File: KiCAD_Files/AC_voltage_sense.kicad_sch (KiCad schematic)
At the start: 18 parts, among them U501 AMC1301DWR, U502 MCP6486UT-E/LT

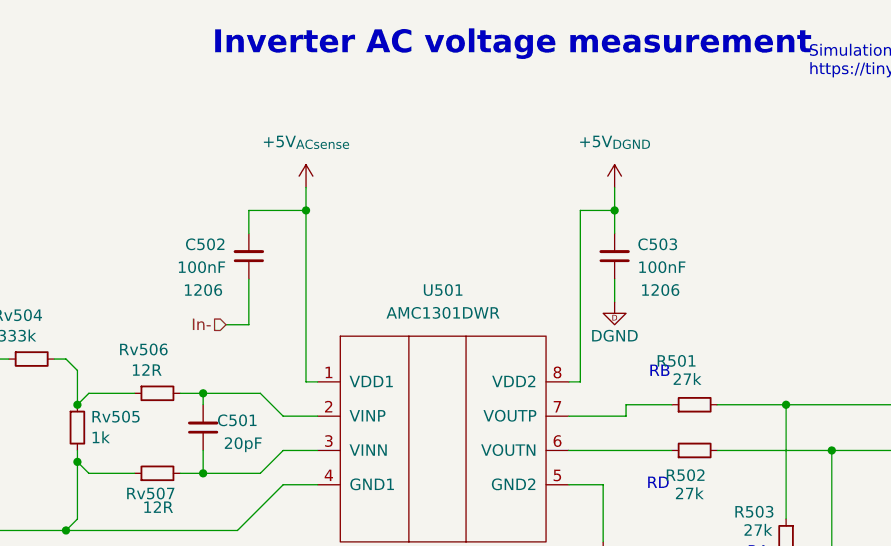
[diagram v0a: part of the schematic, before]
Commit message: First routing pass complete.
Signed-off-by: Jean Alinei <jean.alinei@owntech.org>
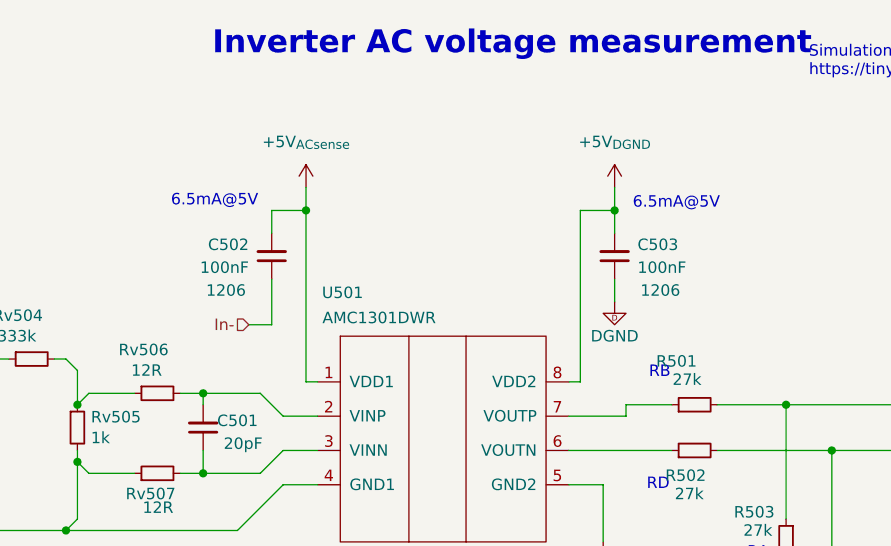
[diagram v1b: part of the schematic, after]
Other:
- note added: "6.5mA@5V"
- moved on the sheet: C502
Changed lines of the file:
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@@
+		)
+	)
+	(text "6.5mA@5V"
+		(exclude_from_sim no)
+		(at 74.93 47.244 0)
+		(effects
+			(font
+				(size 1.27 1.27)
+				(color 194 0 0 1)
+			)
+		)
+	)
+	(text "6.5mA@5V"
+		(exclude_from_sim no)
+		(at 126.238 47.498 0)
+		(effects
+			(font
+				(size 1.27 1.27)
+				(color 194 0 0 1)
+			)
 		)
 	)
@@
 	(wire
 		(pts
-			(xy 78.74 48.26) (xy 78.74 50.8)
+			(xy 81.28 48.26) (xy 81.28 50.8)
 		)
 		(stroke
@@
 	(wire
 		(pts
-			(xy 78.74 60.96) (xy 76.2 60.96)
+			(xy 81.28 60.96) (xy 78.74 60.96)
 		)
 		(stroke
@@
 	(wire
 		(pts
-			(xy 78.74 55.88) (xy 78.74 60.96)
+			(xy 81.28 55.88) (xy 81.28 60.96)
 		)
 		(stroke
@@
 	(wire
 		(pts
-			(xy 78.74 48.26) (xy 85.09 48.26)
+			(xy 81.28 48.26) (xy 85.09 48.26)
 		)
 		(stroke
@@
 	(hierarchical_label "In-"
 		(shape input)
-		(at 76.2 60.96 180)
+		(at 78.74 60.96 180)
 		(effects
 			(font
@@
 			)
 			(justify right)
+		)
+	)
+	(rule_area
+		(polyline
+			(pts
+				(xy 100.33 35.56) (xy 100.33 107.95) (xy 195.58 107.95) (xy 195.58 35.56)
+			)
+			(stroke
+				(width 0)
+				(type dash)
+			)
+			(fill
+				(type none)
+			)
+		)
+	)
+	(netclass_flag ""
+		(length 2.54)
+		(shape round)
+		(at 110.49 107.95 0)
+		(fields_autoplaced yes)
+		(effects
+			(font
+				(size 1.27 1.27)
+			)
+			(justify left bottom)
+		)
+		(property "Netclass" "DGND"
+			(at 111.1885 105.41 0)
+			(effects
+				(font
+					(size 1.27 1.27)
+				)
+				(justify left)
+			)
+		)
+		(property "Component Class" ""
+			(at -148.59 59.69 0)
+			(effects
+				(font
+					(size 1.27 1.27)
+					(italic yes)
+				)
+				(hide yes)
+			)
 		)
 	)
@@
 		(on_board yes)
 		(dnp no)
-		(fields_autoplaced yes)
 		(property "Reference" "U501"
-			(at 100.33 57.15 0)
+			(at 89.154 57.404 0)
 			(effects
 				(font
@@
 		)
 		(property "Value" "AMC1301DWR"
-			(at 100.33 59.69 0)
+			(at 93.218 60.198 0)
 			(effects
 				(font
@@
 			)
 		)
-		(property "Datasheet" "https://www.ti.com/lit/ds/symlink/amc1100.pdf?ts=1597048467257&ref_url=https%253A%252F%252Fwww.google.com%252F"
+		(property "Datasheet" "${KIPRJMOD}\\datasheets\\amc1301.pdf"
 			(at 100.33 81.28 0)
 			(effects
@@
 	(symbol
 		(lib_id "Device:C_Small")
-		(at 78.74 53.34 180)
+		(at 81.28 53.34 180)
 		(unit 1)
 		(exclude_from_sim no)
@@
 		(dnp no)
 		(property "Reference" "C502"
-			(at 76.2 52.07 0)
+			(at 78.74 52.07 0)
 			(effects
 				(font
@@
 		)
 		(property "Value" "100nF"
-			(at 76.2 54.61 0)
+			(at 78.74 54.61 0)
 			(effects
 				(font
@@
 		)
 		(property "Footprint" "Capacitor_SMD:C_1206_3216Metric"
-			(at 78.74 53.34 0)
+			(at 81.28 53.34 0)
 			(effects
 				(font
@@
 		)
 		(property "Datasheet" "${KIPRJMOD}\\datasheet\\KEM_C1002_X7R_SMD-3316098.pdf"
-			(at 78.74 53.34 0)
+			(at 81.28 53.34 0)
 			(effects
 				(font
@@
 		)
 		(property "Description" ""
-			(at 78.74 53.34 0)
+			(at 81.28 53.34 0)
 			(effects
 				(font
@@
 		)
 		(property "manf#" "C1206C104K5RAC7867"
-			(at 78.74 53.34 0)
+			(at 81.28 53.34 0)
 			(effects
 				(font
@@
 		)
 		(property "DNP" ""
-			(at 78.74 53.34 0)
+			(at 81.28 53.34 0)
 			(effects
 				(font
@@
 		)
 		(property "Voltage" "50V"
-			(at 80.01 49.53 90)
+			(at 82.55 49.53 90)
 			(effects
 				(font
@@
 		)
 		(property "Package" "1206"
-			(at 73.66 57.15 0)
+			(at 76.2 57.15 0)
 			(effects
 				(font
@@
 		)
 		(property "Functional Block" "Measurement"
-			(at 78.74 53.34 0)
+			(at 81.28 53.34 0)
 			(effects
 				(font
@@
 		)
 		(property "Metal content" "BaTiO3"
-			(at 78.74 53.34 0)
+			(at 81.28 53.34 0)
 			(effects
 				(font
@@
 		)
 		(property "Subfunction" "VIHigh measure"
-			(at 78.74 53.34 0)
+			(at 81.28 53.34 0)
 			(effects
 				(font
@@
 		)
 		(property "Dielectric" "X7R"
-			(at 78.74 53.34 0)
+			(at 81.28 53.34 0)
 			(effects
 				(font
@@
 		)
 		(property "Technology" ""
-			(at 78.74 53.34 0)
+			(at 81.28 53.34 0)
 			(effects
 				(font
@@
 		)
 		(property "LCSC" "C5449000"
-			(at 78.74 53.34 0)
-			(effects
-				(font
+			(at 81.28 53.34 0)
+			(effects
+				(font

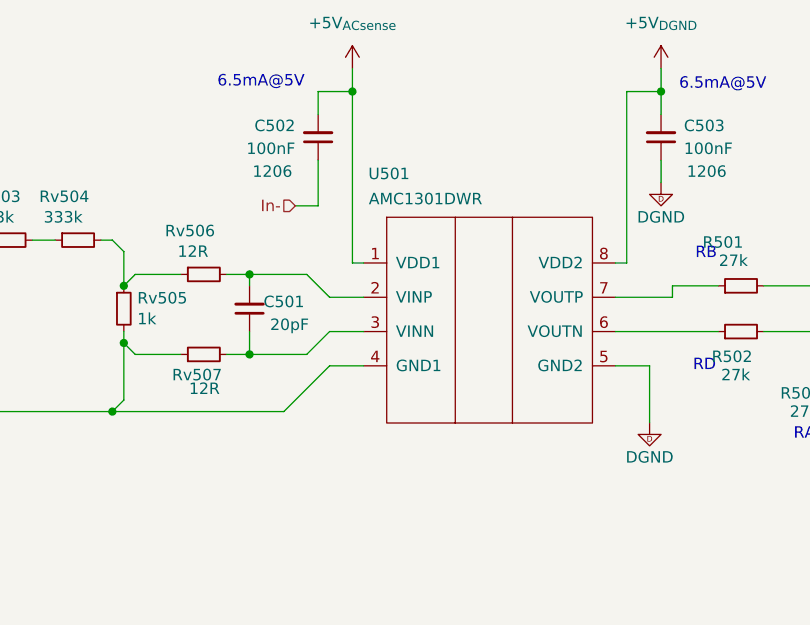
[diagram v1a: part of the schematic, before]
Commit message: Added DRC rules according to IEC60664 and IPC2221.
Signed-off-by: Jean Alinei <jean.alinei@owntech.org>
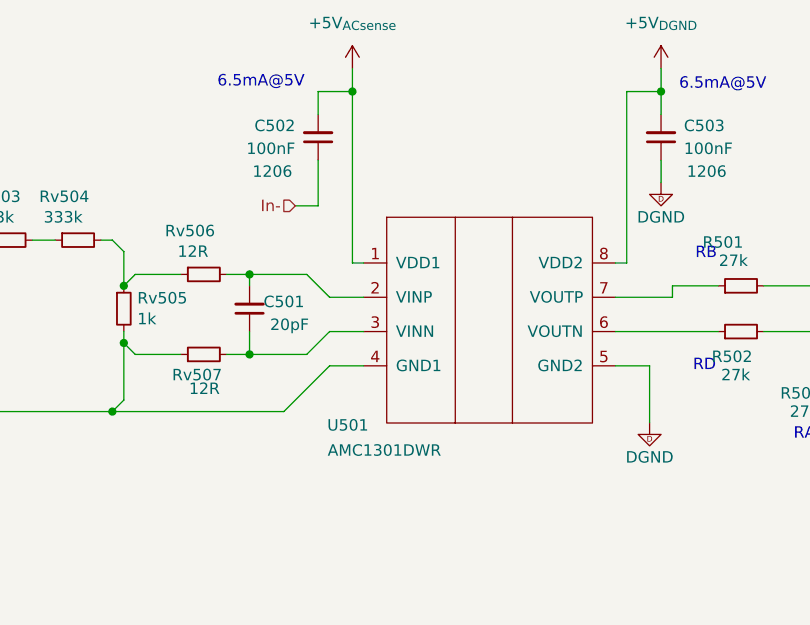
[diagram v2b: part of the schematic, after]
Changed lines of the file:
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@@
 		(polyline
 			(pts
-				(xy 100.33 35.56) (xy 100.33 107.95) (xy 195.58 107.95) (xy 195.58 35.56)
+				(xy 97.79 107.95) (xy 97.79 35.56) (xy 20.32 35.56) (xy 20.32 71.755) (xy 20.32 74.93) (xy 20.32 107.95)
 			)
 			(stroke
@@
 		)
 	)
+	(rule_area
+		(polyline
+			(pts
+				(xy 101.6 35.56) (xy 101.6 107.95) (xy 196.85 107.95) (xy 196.85 35.56)
+			)
+			(stroke
+				(width 0)
+				(type dash)
+			)
+			(fill
+				(type none)
+			)
+		)
+	)
 	(netclass_flag ""
 		(length 2.54)
 		(shape round)
-		(at 110.49 107.95 0)
+		(at 87.63 107.95 0)
 		(fields_autoplaced yes)
 		(effects
@@
 			(justify left bottom)
 		)
+		(property "Netclass" "N"
+			(at 88.3285 105.41 0)
+			(effects
+				(font
+					(size 1.27 1.27)
+				)
+				(justify left)
+			)
+		)
+		(property "Component Class" ""
+			(at -171.45 59.69 0)
+			(effects
+				(font
+					(size 1.27 1.27)
+					(italic yes)
+				)
+				(hide yes)
+			)
+		)
+	)
+	(netclass_flag ""
+		(length 2.54)
+		(shape round)
+		(at 111.76 107.95 0)
+		(fields_autoplaced yes)
+		(effects
+			(font
+				(size 1.27 1.27)
+			)
+			(justify left bottom)
+		)
 		(property "Netclass" "DGND"
-			(at 111.1885 105.41 0)
+			(at 112.4585 105.41 0)
 			(effects
 				(font
@@
 		)
 		(property "Component Class" ""
-			(at -148.59 59.69 0)
+			(at -147.32 59.69 0)
 			(effects
 				(font
@@
 		(dnp no)
 		(property "Reference" "U501"
-			(at 89.154 57.404 0)
+			(at 84.582 85.344 0)
 			(effects
 				(font
@@
 		)
 		(property "Value" "AMC1301DWR"
-			(at 93.218 60.198 0)
-			(effects
-				(font
+			(at 88.646 88.138 0)
+			(effects
+				(font

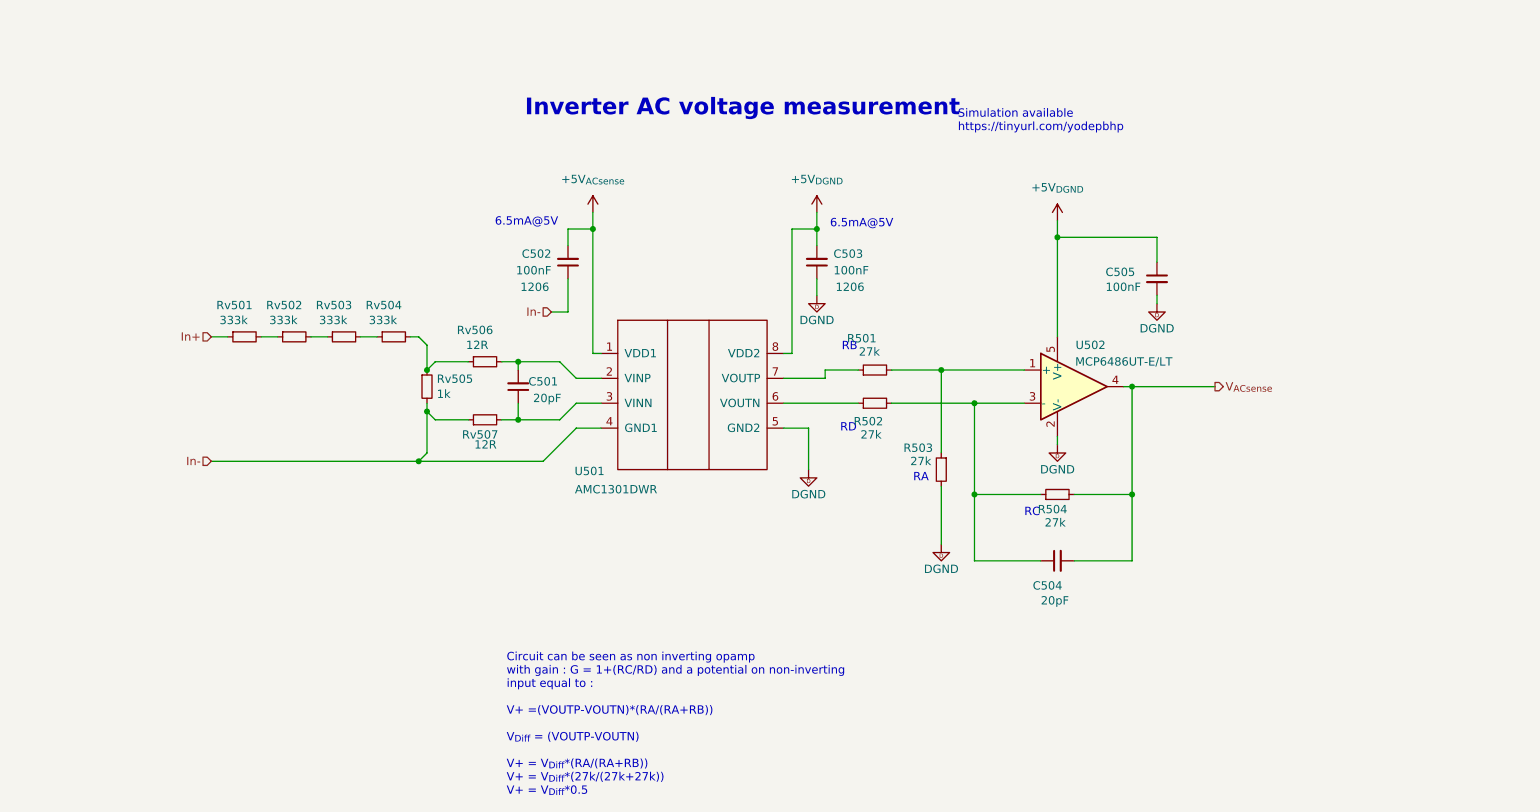
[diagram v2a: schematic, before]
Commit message: Added passive references. Added ESD protection for MCU pins.
Signed-off-by: Jean Alinei <jean.alinei@owntech.org>
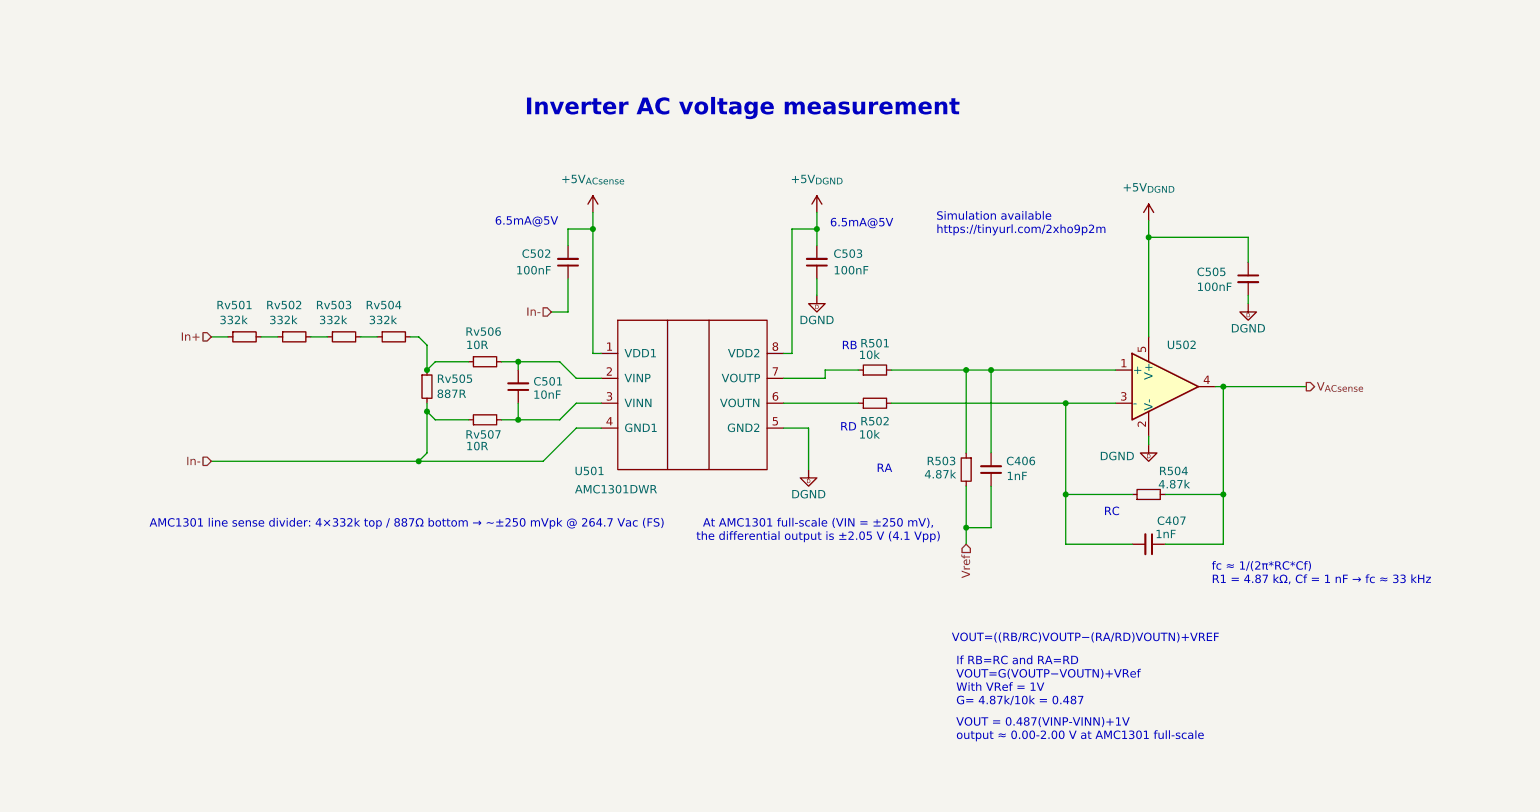
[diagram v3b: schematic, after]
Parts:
- removed C504: 20pF, Footprints:C_0805_2012Metric, symbol Device:C_Small
- added C406, C407: 1nF, Footprints:C_0805_2012Metric, symbol Device:C_Small
- C501: value 20pF -> 10nF; Dielectric NP0 -> (none); LCSC (none) -> C1710; Package 0805 -> (none); Voltage 50V -> (none); manf# CC0805JRNPO9BN200 -> (none)
- C502, C503: Dielectric X7R -> (none); LCSC C5449000 -> C24497; Metal content BaTiO3 -> (none); Package 1206 -> (none); Subfunction VIHigh measure -> (none); Voltage 50V -> (none); manf# C1206C104K5RAC7867 -> (none)
- C505: Dielectric X7R -> (none); LCSC C5449000 -> C49678; Package 1206 -> (none); Voltage 50V -> (none); manf# C1206C104K5RAC7867 -> (none)
- R501, R502: value 27k -> 10k; LCSC (none) -> C17414; Package 0805 -> (none); Technology Thin film -> (none); manf# RT0805DRD0727KL -> (none)
- R503, R504: value 27k -> 4.87k; LCSC (none) -> C228870; Package 0805 -> (none); Technology Thin film -> (none); manf# RT0805DRD0727KL -> (none)
- Rv501, Rv502, Rv503, Rv504: value 333k -> 332k; LCSC (none) -> C5713304
- Rv505: value 1k -> 887R; LCSC (none) -> C144545
- Rv506, Rv507: value 12R -> 10R; LCSC (none) -> C17415
- U502: Rotation Offset (none) -> 90; Subfunction IILow Measure -> (none); manf# MCP6486UT-E/LT -> (none)
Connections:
- net DGND: no longer R503.2
- net V_{ACsense}: now also C407.1
- net at R501.2, R503.1, U502.1 (+): now also C406.2
- net at R502.2, R504.1, U502.3 (-): now also C407.2
- new net Vref: C406.1, R503.2
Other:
- note added: "AMC1301 line sense divider: 4×332k top / 887Ω bottom → ~±250 mVpk @ 264.7 Vac (FS)"
- note added: "At AMC1301 full-scale (VIN = ±250 mV), the differential output is ±2.05 V (4.1 Vpp)"
- note added: "If RB=RC and RA=RD VOUT​=G(VOUTP​−VOUTN​)+VRef With VRef = 1V G= 4.87k/10k = 0.487"
- note added: "Simulation available https://tinyurl.com/2xho9p2m"
- note added: "VOUT = 0.487(VINP-VINN)+1V output ≈ 0.00-2.00 V at AMC1301 full-scale"
- note added: "VOUT​=((RB/RC)VOUTP​−(RA/RD)VOUTN​)+VREF​"
- note added: "fc ​≈ 1/(2π*RC*Cf)​ R1 = 4.87 kΩ, Cf = 1 nF → fc ≈ 33 kHz"
- note removed: "Circuit can be seen as non inverting opamp with gain : G = 1+(RC/RD) and a potential on non-inverting input equal to : V+ =(VOUTP-VOUTN)*(RA/(RA+RB)) V_{Diff} = (VOUTP-VOUTN) V+ = V_{Diff}*(RA/(RA+RB)) V+ = V_{Diff}*(27k/(27k+27k)) V+ = V_{Diff}*0.5"
- note removed: "Simulation available https://tinyurl.com/yodepbhp"
- moved on the sheet: C505, R503, R504, U502
